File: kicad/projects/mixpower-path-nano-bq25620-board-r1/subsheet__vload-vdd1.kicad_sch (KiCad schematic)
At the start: 13 parts, among them Q8 SIA931DJ, Q9 Si1026X

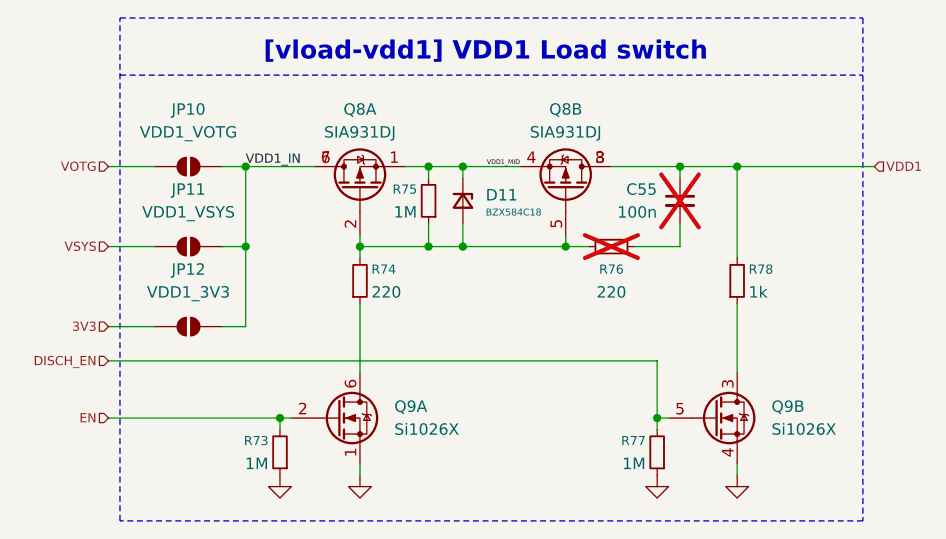
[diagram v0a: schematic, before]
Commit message: fix: put all subsheets in root of the Kicad project, regenerate schematics plots
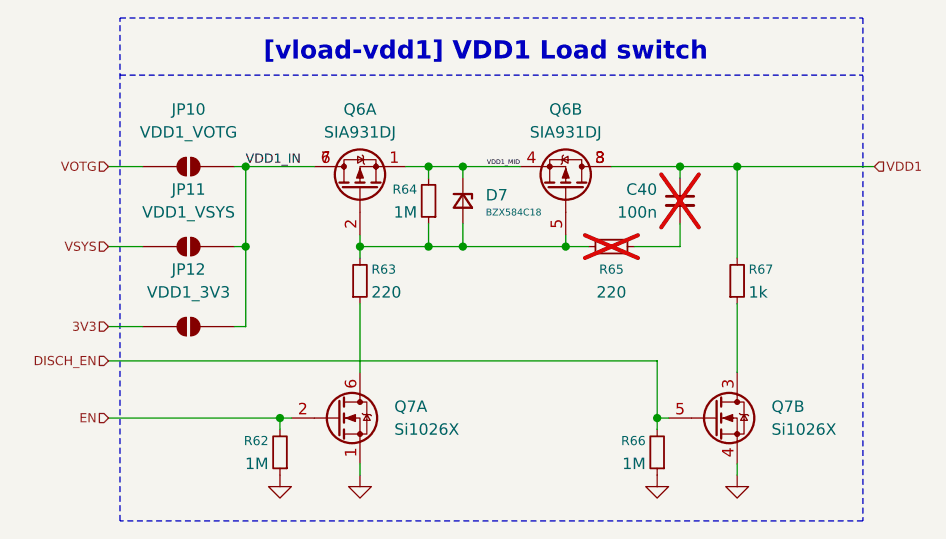
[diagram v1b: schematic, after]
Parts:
- renumbered C55 to C40, D11 to D7, Q8 to Q6, Q9 to Q7, R73 to R62, R74 to R63, R75 to R64, R76 to R65, R77 to R66, R78 to R67
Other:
- title: (none) -> mixpower-path-nano-bq25620-board
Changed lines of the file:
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@@
 	(generator_version "10.0")
 	(paper "A4")
+	(title_block
+		(title "mixpower-path-nano-bq25620-board")
+		(date "2026-04-05")
+		(rev "R1")
+	)
 	(rectangle
 		(start 92.71 58.42)
@@
 	)
 	(junction
-		(at 106.68 83.82)
-		(diameter 0)
-		(color 0 0 0 0)
-	)
-	(junction
 		(at 127 83.82)
 		(diameter 0)
@@
 	)
 	(junction
-		(at 106.68 74.93)
+		(at 127 74.93)
 		(diameter 0)
 		(color 0 0 0 0)
 	)
 	(junction
-		(at 127 74.93)
+		(at 106.68 83.82)
 		(diameter 0)
 		(color 0 0 0 0)
@@
 		(color 0 0 0 0)
 	)
-	(wire
-		(pts
-			(xy 91.44 74.93) (xy 96.52 74.93)
-		)
-		(stroke
-			(width 0)
-			(type default)
-		)
+	(junction
+		(at 106.68 74.93)
+		(diameter 0)
+		(color 0 0 0 0)
 	)
 	(wire
@@
 	(wire
 		(pts
-			(xy 91.44 83.82) (xy 96.52 83.82)
+			(xy 91.44 74.93) (xy 95.25 74.93)
 		)
 		(stroke
@@
 	(wire
 		(pts
-			(xy 104.14 92.71) (xy 106.68 92.71)
-		)
-		(stroke
-			(width 0)
-			(type default)
-		)
-	)
-	(wire
-		(pts
 			(xy 142.24 82.55) (xy 142.24 83.82)
 		)
@@
 	(wire
 		(pts
+			(xy 105.41 83.82) (xy 106.68 83.82)
+		)
+		(stroke
+			(width 0)
+			(type default)
+		)
+	)
+	(wire
+		(pts
 			(xy 161.29 109.22) (xy 161.29 107.95)
 		)
@@
 	(wire
 		(pts
+			(xy 105.41 74.93) (xy 106.68 74.93)
+		)
+		(stroke
+			(width 0)
+			(type default)
+		)
+	)
+	(wire
+		(pts
 			(xy 152.4 96.52) (xy 152.4 102.87)
 		)
@@
 	(wire
 		(pts
+			(xy 105.41 92.71) (xy 106.68 92.71)
+		)
+		(stroke
+			(width 0)
+			(type default)
+		)
+	)
+	(wire
+		(pts
 			(xy 119.38 83.82) (xy 119.38 85.09)
 		)
@@
 	(wire
 		(pts
-			(xy 91.44 92.71) (xy 96.52 92.71)
+			(xy 91.44 92.71) (xy 95.25 92.71)
 		)
 		(stroke
@@
 		(pts
 			(xy 130.81 74.93) (xy 137.16 74.93)
-		)
-		(stroke
-			(width 0)
-			(type default)
-		)
-	)
-	(wire
-		(pts
-			(xy 104.14 83.82) (xy 106.68 83.82)
 		)
 		(stroke
@@
 	(wire
 		(pts
+			(xy 91.44 83.82) (xy 95.25 83.82)
+		)
+		(stroke
+			(width 0)
+			(type default)
+		)
+	)
+	(wire
+		(pts
 			(xy 127 74.93) (xy 127 76.2)
 		)
@@
 		(pts
 			(xy 119.38 82.55) (xy 119.38 83.82)
-		)
-		(stroke
-			(width 0)
-			(type default)
-		)
-	)
-	(wire
-		(pts
-			(xy 104.14 74.93) (xy 106.68 74.93)
 		)
 		(stroke
@@
 		(in_pos_files yes)
 		(dnp no)
-		(property "Reference" "R78"
+		(property "Reference" "R67"
 			(at 162.56 86.3599 0)
 			(show_name no)
@@
 			(project "mixpower-path-nano-bq25620-board-r1"
 				(path "/2e43857b-9bf9-460c-948c-ec2cf8a8d6b4/58d5e6bb-811f-45d3-aa67-b144100f4607"
-					(reference "R78")
+					(reference "R67")
 					(unit 1)
 				)
@@
 		(in_pos_files yes)
 		(dnp yes)
-		(property "Reference" "C55"
+		(property "Reference" "C40"
 			(at 152.4 77.4762 0)
 			(show_name no)
@@
 			(project "mixpower-path-nano-bq25620-board-r1"
 				(path "/2e43857b-9bf9-460c-948c-ec2cf8a8d6b4/58d5e6bb-811f-45d3-aa67-b144100f4607"
-					(reference "C55")
+					(reference "C40")
 					(unit 1)
 				)
@@
 		(dnp no)
 		(fields_autoplaced yes)
-		(property "Reference" "#PWR095"
+		(property "Reference" "#PWR068"
 			(at 152.4 115.57 0)
 			(hide yes)
@@
 			(project "mixpower-path-nano-bq25620-board-r1"
 				(path "/2e43857b-9bf9-460c-948c-ec2cf8a8d6b4/58d5e6bb-811f-45d3-aa67-b144100f4607"
-					(reference "#PWR095")
+					(reference "#PWR068")
 					(unit 1)
 				)
@@
 		(in_pos_files yes)
 		(dnp no)
-		(property "Reference" "Q8"
+		(property "Reference" "Q6"
 			(at 142.24 68.58 90)
 			(show_name no)
@@
 			(project "mixpower-path-nano-bq25620-board-r1"
 				(path "/2e43857b-9bf9-460c-948c-ec2cf8a8d6b4/58d5e6bb-811f-45d3-aa67-b144100f4607"
-					(reference "Q8")
+					(reference "Q6")
 					(unit 2)
 				)
@@
 		(in_pos_files yes)
 		(dnp no)
-		(property "Reference" "R73"
+		(property "Reference" "R62"
 			(at 109.22 105.4099 0)
 			(show_name no)
@@
 			(project "mixpower-path-nano-bq25620-board-r1"
 				(path "/2e43857b-9bf9-460c-948c-ec2cf8a8d6b4/58d5e6bb-811f-45d3-aa67-b144100f4607"
-					(reference "R73")
+					(reference "R62")
 					(unit 1)
 				)
@@
 		(dnp no)
 		(fields_autoplaced yes)
-		(property "Reference" "#PWR093"
+		(property "Reference" "#PWR066"
 			(at 110.49 115.57 0)
 			(hide yes)
@@
 			(project "mixpower-path-nano-bq25620-board-r1"
 				(path "/2e43857b-9bf9-460c-948c-ec2cf8a8d6b4/58d5e6bb-811f-45d3-aa67-b144100f4607"
-					(reference "#PWR093")
+					(reference "#PWR066")
 					(unit 1)
 				)
@@
 		(dnp yes)
 		(fields_autoplaced yes)
-		(property "Reference" "R76"
+		(property "Reference" "R65"
 			(at 147.32 86.36 90)
 			(show_name no)
@@
 			(project "mixpower-path-nano-bq25620-board-r1"
 				(path "/2e43857b-9bf9-460c-948c-ec2cf8a8d6b4/58d5e6bb-811f-45d3-aa67-b144100f4607"
-					(reference "R76")
+					(reference "R65")
 					(unit 1)
 				)
@@
 		(in_pos_files yes)
 		(dnp no)
-		(property "Reference" "R77"
+		(property "Reference" "R66"
 			(at 151.13 105.4099 0)
 			(show_name no)
@@
 			(project "mixpower-path-nano-bq25620-board-r1"
 				(path "/2e43857b-9bf9-460c-948c-ec2cf8a8d6b4/58d5e6bb-811f-45d3-aa67-b144100f4607"
-					(reference "R77")
+					(reference "R66")
 					(unit 1)
 				)
@@
 		(dnp no)
 		(fields_autoplaced yes)
-		(property "Reference" "#PWR096"
+		(property "Reference" "#PWR069"
 			(at 161.29 115.57 0)
 			(hide yes)
@@
 			(project "mixpower-path-nano-bq25620-board-r1"
 				(path "/2e43857b-9bf9-460c-948c-ec2cf8a8d6b4/58d5e6bb-811f-45d3-aa67-b144100f4607"
-					(reference "#PWR096")
+					(reference "#PWR069")
 					(unit 1)
 				)
@@
 		(in_pos_files yes)
 		(dnp no)
-		(property "Reference" "R75"
+		(property "Reference" "R64"
 			(at 125.73 77.4699 0)
 			(show_name no)
@@
 			(project "mixpower-path-nano-bq25620-board-r1"
 				(path "/2e43857b-9bf9-460c-948c-ec2cf8a8d6b4/58d5e6bb-811f-45d3-aa67-b144100f4607"
-					(reference "R75")
+					(reference "R64")
 					(unit 1)
 				)
@@
 	)
 	(symbol
+		(lib_name "SolderJumper_2_Open_2")
 		(lib_id "Jumper:SolderJumper_2_Open")
 		(at 100.33 83.82 0)
@@
 		(in_pos_files yes)
 		(dnp no)
-		(property "Reference" "R74"
+		(property "Reference" "R63"
 			(at 120.65 86.3599 0)
 			(show_name no)
@@
 			(project "mixpower-path-nano-bq25620-board-r1"
 				(path "/2e43857b-9bf9-460c-948c-ec2cf8a8d6b4/58d5e6bb-811f-45d3-aa67-b144100f4607"
-					(reference "R74")
+					(reference "R63")
 					(unit 1)
 				)
@@
 		(dnp no)
 		(fields_autoplaced yes)
-		(property "Reference" "Q9"
+		(property "Reference" "Q7"
 			(at 123.19 101.5999 0)
 			(show_name no)
@@
 			(project "mixpower-path-nano-bq25620-board-r1"
 				(path "/2e43857b-9bf9-460c-948c-ec2cf8a8d6b4/58d5e6bb-811f-45d3-aa67-b144100f4607"
-					(reference "Q9")
+					(reference "Q7")
 					(unit 1)
 				)
@@
 		(dnp no)
 		(fields_autoplaced yes)
-		(property "Reference" "D11"
+		(property "Reference" "D7"
 			(at 133.35 78.1049 90)
 			(show_name no)
@@
 			(project "mixpower-path-nano-bq25620-board-r1"
 				(path "/2e43857b-9bf9-460c-948c-ec2cf8a8d6b4/58d5e6bb-811f-45d3-aa67-b144100f4607"
-					(reference "D11")
+					(reference "D7")
 					(unit 1)
 				)
@@
 		(in_pos_files yes)
 		(dnp no)
-		(property "Reference" "Q8"
+		(property "Reference" "Q6"
 			(at 119.38 68.58 90)
 			(show_name no)
@@
 			(project "mixpower-path-nano-bq25620-board-r1"
 				(path "/2e43857b-9bf9-460c-948c-ec2cf8a8d6b4/58d5e6bb-811f-45d3-aa67-b144100f4607"
-					(reference "Q8")
+					(reference "Q6")
 					(unit 1)
 				)
@@
 	)
 	(symbol
+		(lib_name "SolderJumper_2_Open_1")
 		(lib_id "Jumper:SolderJumper_2_Open")
 		(at 100.33 74.93 0)
@@
 		(dnp no)
 		(fields_autoplaced yes)
-		(property "Reference" "Q9"
+		(property "Reference" "Q7"
 			(at 165.1 101.5999 0)
 			(show_name no)
@@
 			(project "mixpower-path-nano-bq25620-board-r1"
 				(path "/2e43857b-9bf9-460c-948c-ec2cf8a8d6b4/58d5e6bb-811f-45d3-aa67-b144100f4607"
-					(reference "Q9")
+					(reference "Q7")
 					(unit 2)
 				)
@@
 		(dnp no)
 		(fields_autoplaced yes)
-		(property "Reference" "#PWR094"
+		(property "Reference" "#PWR067"
 			(at 119.38 115.57 0)
 			(hide yes)
@@
 			(project "mixpower-path-nano-bq25620-board-r1"
 				(path "/2e43857b-9bf9-460c-948c-ec2cf8a8d6b4/58d5e6bb-811f-45d3-aa67-b144100f4607"
-					(reference "#PWR094")
+					(reference "#PWR067")
 					(unit 1)
 				)
